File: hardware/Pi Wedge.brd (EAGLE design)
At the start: 55.9 x 49.5 mm, 15 parts

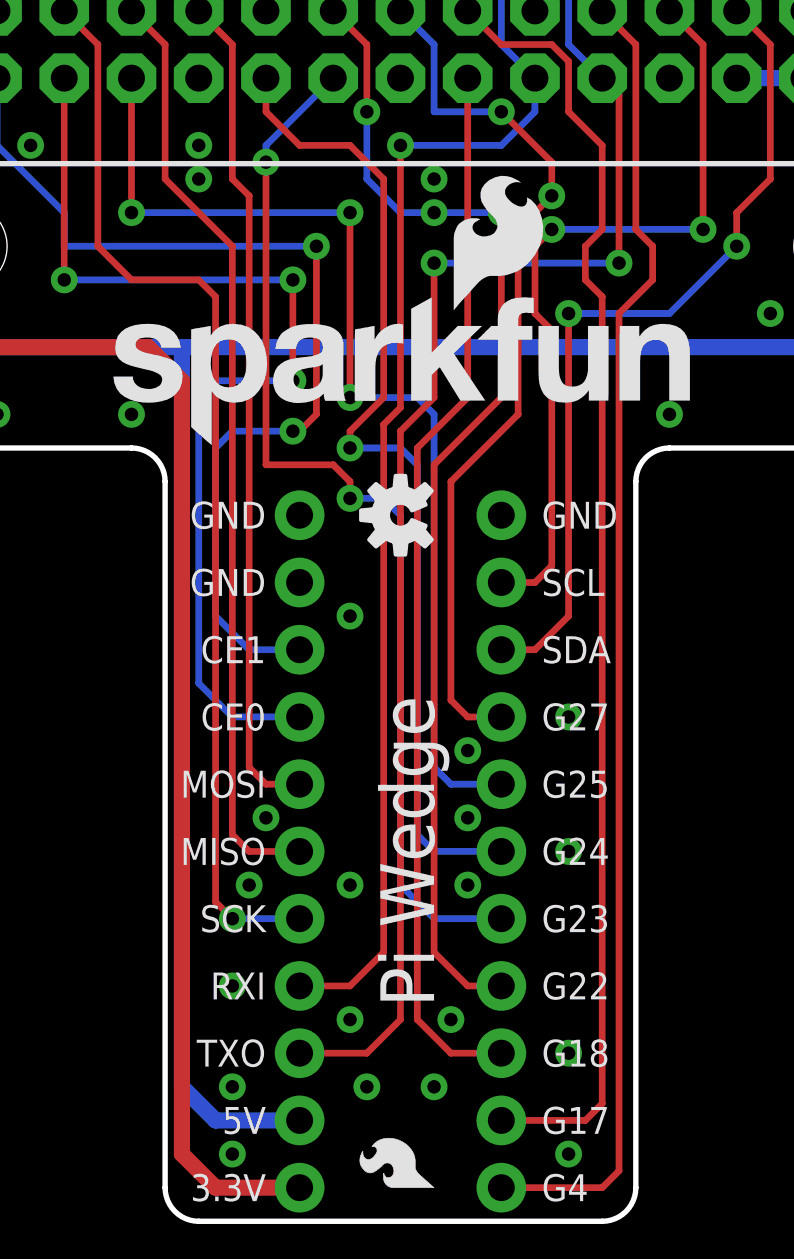
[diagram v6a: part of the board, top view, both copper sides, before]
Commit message: Moving vias from under silk.
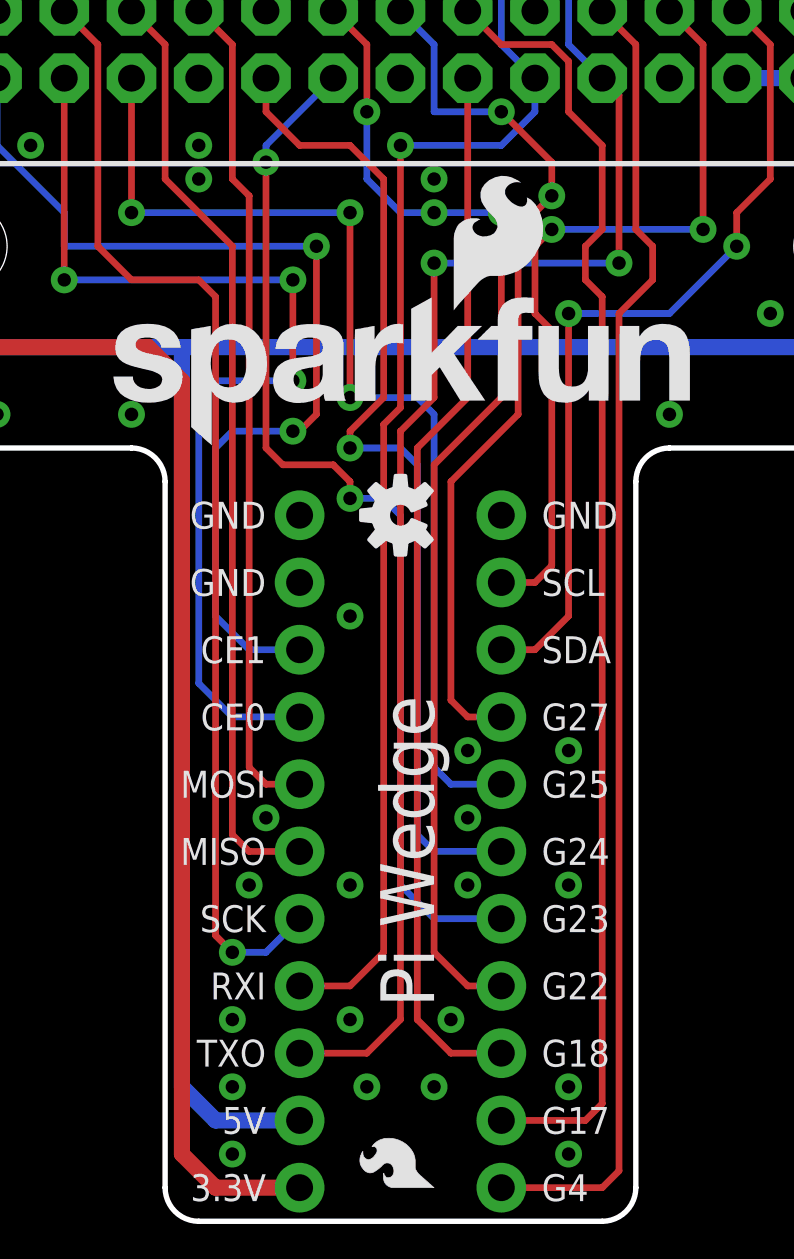
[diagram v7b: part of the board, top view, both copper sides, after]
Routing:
- net SCLK: track 40.9 -> 42.7 mm
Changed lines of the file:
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@@
 <via x="16.51" y="30.48" extent="1-16" drill="0.508"/>
 <via x="26.67" y="47.625" extent="1-16" drill="0.508"/>
-<via x="20.32" y="8.89" extent="1-16" drill="0.508"/>
+<via x="20.32" y="7.62" extent="1-16" drill="0.508"/>
 <via x="20.32" y="5.08" extent="1-16" drill="0.508"/>
 <via x="25.4" y="5.08" extent="1-16" drill="0.508"/>
@@
 <via x="19.05" y="40.64" extent="1-16" drill="0.508"/>
 <via x="19.05" y="39.37" extent="1-16" drill="0.508"/>
-<via x="33.02" y="6.35" extent="1-16" drill="0.508"/>
-<via x="33.02" y="13.97" extent="1-16" drill="0.508"/>
-<via x="33.02" y="19.05" extent="1-16" drill="0.508"/>
+<via x="33.02" y="5.08" extent="1-16" drill="0.508"/>
+<via x="33.02" y="12.7" extent="1-16" drill="0.508"/>
+<via x="33.02" y="17.78" extent="1-16" drill="0.508"/>
 <via x="12.7" y="40.64" extent="1-16" drill="0.508"/>
 <via x="29.21" y="17.78" extent="1-16" drill="0.508"/>
@@
 <contactref element="JP8" pad="23"/>
 <contactref element="JP11" pad="5"/>
-<wire x1="22.86" y1="11.43" x2="20.32" y2="11.43" width="0.254" layer="16"/>
-<wire x1="20.32" y1="11.43" x2="19.685" y2="12.065" width="0.254" layer="1"/>
-<wire x1="19.685" y1="12.065" x2="19.685" y2="34.925" width="0.254" layer="1"/>
+<wire x1="22.86" y1="11.43" x2="21.59" y2="10.16" width="0.254" layer="16"/>
+<wire x1="21.59" y1="10.16" x2="20.32" y2="10.16" width="0.254" layer="16"/>
+<wire x1="20.32" y1="10.16" x2="19.685" y2="10.795" width="0.254" layer="1"/>
+<wire x1="19.685" y1="10.795" x2="19.685" y2="34.925" width="0.254" layer="1"/>
 <wire x1="13.97" y1="45.72" x2="15.24" y2="44.45" width="0.254" layer="1"/>
 <wire x1="15.24" y1="44.45" x2="15.24" y2="36.83" width="0.254" layer="1"/>
@@
 <wire x1="16.51" y1="35.56" x2="19.05" y2="35.56" width="0.254" layer="1"/>
 <wire x1="19.685" y1="34.925" x2="19.05" y2="35.56" width="0.254" layer="1"/>
-<via x="20.32" y="11.43" extent="1-16" drill="0.508"/>
+<via x="20.32" y="10.16" extent="1-16" drill="0.508"/>
 </signal>
 <signal name="MISO">
@@
 <wire x1="24.765" y1="27.305" x2="24.765" y2="27.94" width="0.254" layer="1"/>
 <wire x1="24.765" y1="27.94" x2="24.13" y2="28.575" width="0.254" layer="1"/>
-<wire x1="24.13" y1="28.575" x2="21.59" y2="28.575" width="0.254" layer="1"/>
-<wire x1="21.59" y1="28.575" x2="21.59" y2="40.005" width="0.254" layer="1"/>
+<wire x1="24.13" y1="28.575" x2="22.225" y2="28.575" width="0.254" layer="1"/>
+<wire x1="22.225" y1="28.575" x2="21.59" y2="29.21" width="0.254" layer="1"/>
+<wire x1="21.59" y1="29.21" x2="21.59" y2="40.005" width="0.254" layer="1"/>
 <via x="21.59" y="40.005" extent="1-16" drill="0.508"/>
 <wire x1="21.59" y1="40.005" x2="21.59" y2="40.64" width="0.254" layer="16"/>

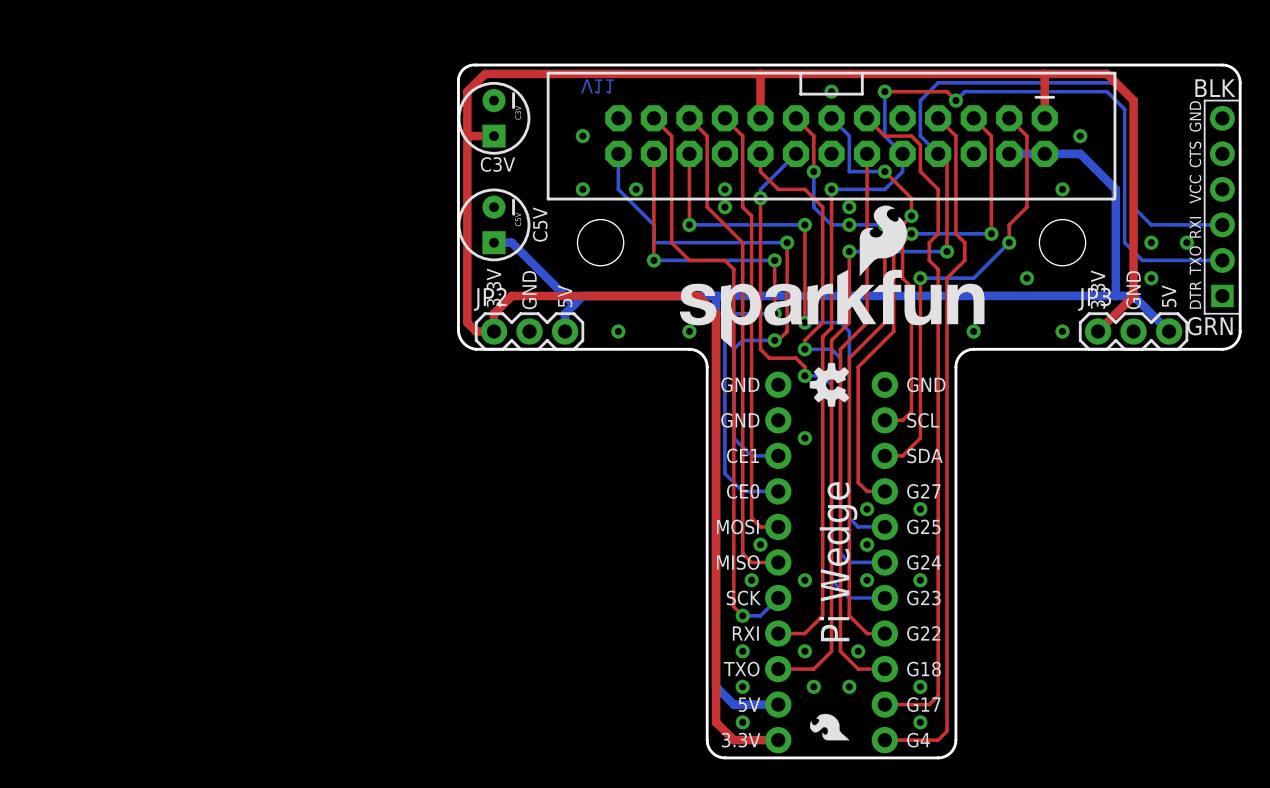
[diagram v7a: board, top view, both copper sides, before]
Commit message: V1.2: Design revisions.
Removing separate 5V and 3.3V connectors.
Integrating 3.3V and 5V in both sides of the DIP-footprint area.
Fixing swapped Tx/Rx on FTDI connector.
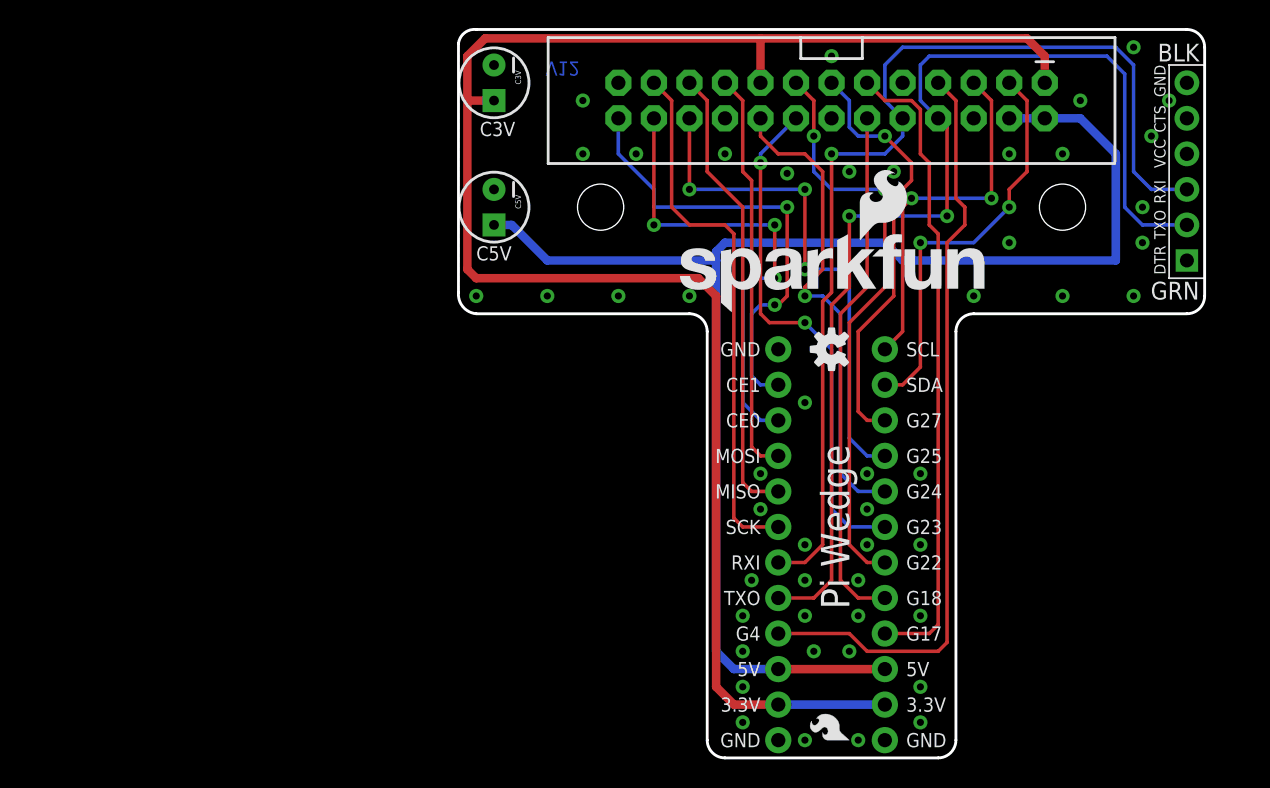
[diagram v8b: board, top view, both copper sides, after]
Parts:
- removed JP11, JP12: 1x11 Header, SparkFun-Connectors:1X11_NO_SILK_KIT
- JP2, JP3: value PWR -> M121X12_NO_SILK_KIT; device SparkFun-Connectors:1X03 -> SparkFun-Connectors:1X12_NO_SILK_KIT
- moved JP2 35.6 mm to (22.9, 1.27), flipped to the bottom, turned to 90 degrees
- moved JP3 32.9 mm to (30.5, 1.27), flipped to the bottom, turned to 90 degrees
- moved JP4 3.59 mm to (52.1, 41.9)
- moved C3V 2.54 mm to (2.54, 48.3)
- moved JP8 2.54 mm to (26.7, 47.0)
- moved LOGO1 2.54 mm to (15.1, 31.8)
- moved STANDOFF1 2.54 mm to (10.2, 39.4)
- moved STANDOFF2 2.54 mm to (43.2, 39.4)
- moved U$1 2.54 mm to (26.7, 29.2)
- moved JP5 2.01 mm to (27.9, 3.17), turned to 270 degrees
- moved C5V 1.27 mm to (2.54, 39.4)
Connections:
- removed net GPIO17: JP12.2, JP8.11
- removed net GPIO18: JP12.3, JP8.12
- removed net GPIO22: JP12.4, JP8.15
- removed net GPIO23: JP12.5, JP8.16
- removed net GPIO24: JP12.6, JP8.18
- removed net GPIO25: JP12.7, JP8.22
- removed net GPIO27: JP12.8, JP8.13
- removed net GPIO4: JP12.1, JP8.7
- new net GP17: JP3.4, JP8.11
- new net GP18: JP3.5, JP8.12
- new net GP22: JP3.6, JP8.15
- new net GP23: JP3.7, JP8.16
- new net GP24: JP3.8, JP8.18
- new net GP25: JP3.9, JP8.22
- new net GP27: JP3.10, JP8.13
- new net GP4: JP2.4, JP8.7
- net 3.3V: now also JP2.2, JP3.2; no longer JP11.1, JP2.1, JP3.1
- net 5V: no longer JP11.2
- net CE0: now also JP2.10; no longer JP11.8
- net CE1: now also JP2.11; no longer JP11.9
- net GND: now also JP2.1, JP2.12, JP3.1; no longer JP11.10, JP11.11, JP12.11, JP2.2, JP3.2
- net MISO: now also JP2.8; no longer JP11.6
- net MOSI: now also JP2.9; no longer JP11.7
- net RXI: now also JP2.6, JP4.P$3; no longer JP11.4, JP4.P$2
- net SCL: now also JP3.12; no longer JP12.10
- net SCLK: now also JP2.7; no longer JP11.5
- net SDA: now also JP3.11; no longer JP12.9
- net TXO: now also JP2.5, JP4.P$2; no longer JP11.3, JP4.P$3
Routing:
- net GP4: track 0.00 -> 54.2 mm
- net GPIO4: track 49.8 -> 0.00 mm
- net GPIO17: track 49.1 -> 0.00 mm
- net GP17: track 0.00 -> 46.0 mm
- net GPIO22: track 44.5 -> 0.00 mm, vias 3 -> 0
- net GP22: track 0.00 -> 42.0 mm, vias 0 -> 2
- net GPIO18: track 40.1 -> 0.00 mm
- net GPIO25: track 39.9 -> 0.00 mm, vias 3 -> 0
- net GPIO23: track 39.8 -> 0.00 mm, vias 2 -> 0
- net GPIO24: track 37.7 -> 0.00 mm, vias 1 -> 0
- net GP18: track 0.00 -> 37.5 mm
- net GP25: track 0.00 -> 37.0 mm, vias 0 -> 3
- net GP23: track 0.00 -> 36.9 mm, vias 0 -> 2
- net GP24: track 0.00 -> 34.4 mm, vias 0 -> 1
- net GPIO27: track 33.6 -> 0.00 mm, vias 2 -> 0
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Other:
- board size 55.9 x 49.5 mm -> 53.3 x 52.1 mm
- board text added: "V12"
- board text removed: "V11"
